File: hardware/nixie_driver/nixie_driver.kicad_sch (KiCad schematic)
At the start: 46 parts, among them J2 Conn_02x05_Odd_Even, U8 CD40109B, U9 TubeClock_HV5622

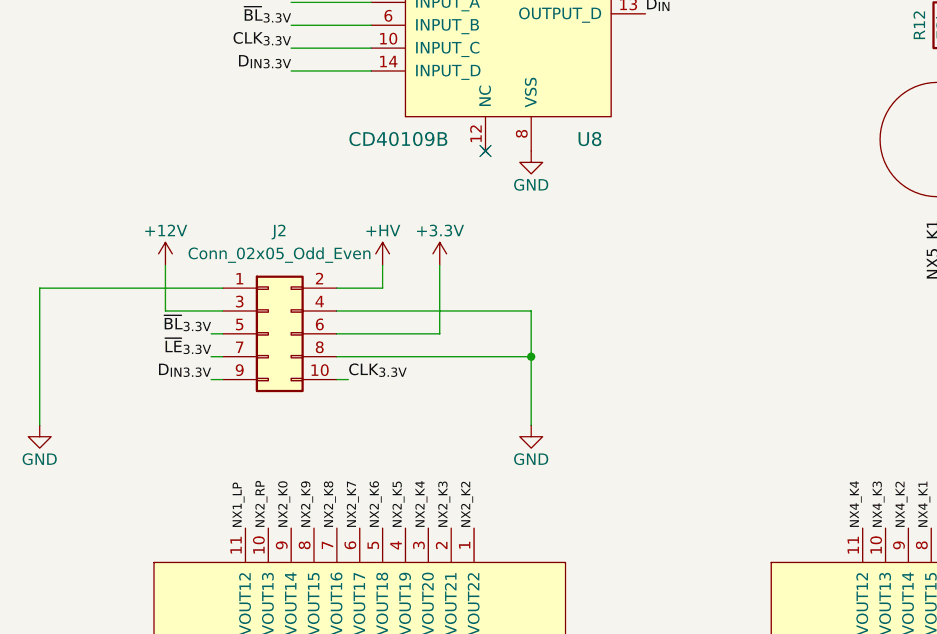
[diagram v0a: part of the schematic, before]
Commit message: Changed connectors to driver board, fixed oscillator connections
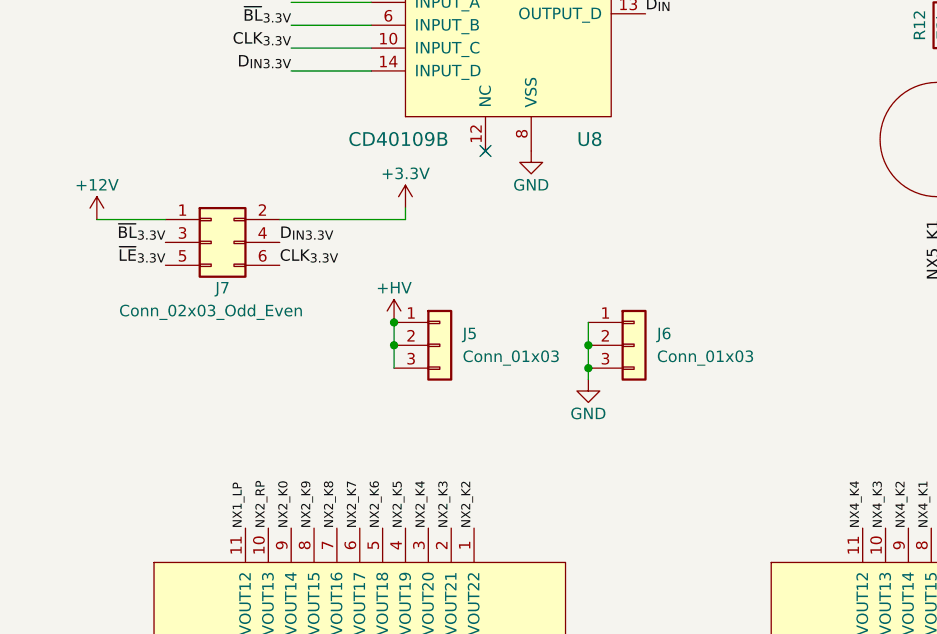
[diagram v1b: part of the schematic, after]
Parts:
- removed J2: Conn_02x05_Odd_Even, Connector_PinHeader_2.54mm:PinHeader_2x05_P2.54mm_Vertical, symbol Connector_Generic:Conn_02x05_Odd_Even
- added J5, J6: Conn_01x03, Connector_PinHeader_2.54mm:PinHeader_1x03_P2.54mm_Vertical, symbol Connector_Generic:Conn_01x03
- added J7: Conn_02x03_Odd_Even, Connector_PinHeader_2.54mm:PinHeader_2x03_P2.54mm_Vertical, symbol Connector_Generic:Conn_02x03_Odd_Even
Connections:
- net +12V: now also J7.1 (Pin_1)
- net +3V3: now also J7.2 (Pin_2)
- net +HV: now also J5.1 (Pin_1), J5.2 (Pin_2), J5.3 (Pin_3)
- net CLK_{3.3V}: now also J7.6 (Pin_6)
- net D_{IN}_{3.3V}: now also J7.4 (Pin_4)
- net GND: now also J6.1 (Pin_1), J6.2 (Pin_2), J6.3 (Pin_3)
- net ~{BL}_{3.3V}: now also J7.3 (Pin_3)
- net ~{LE}_{3.3V}: now also J7.5 (Pin_5)

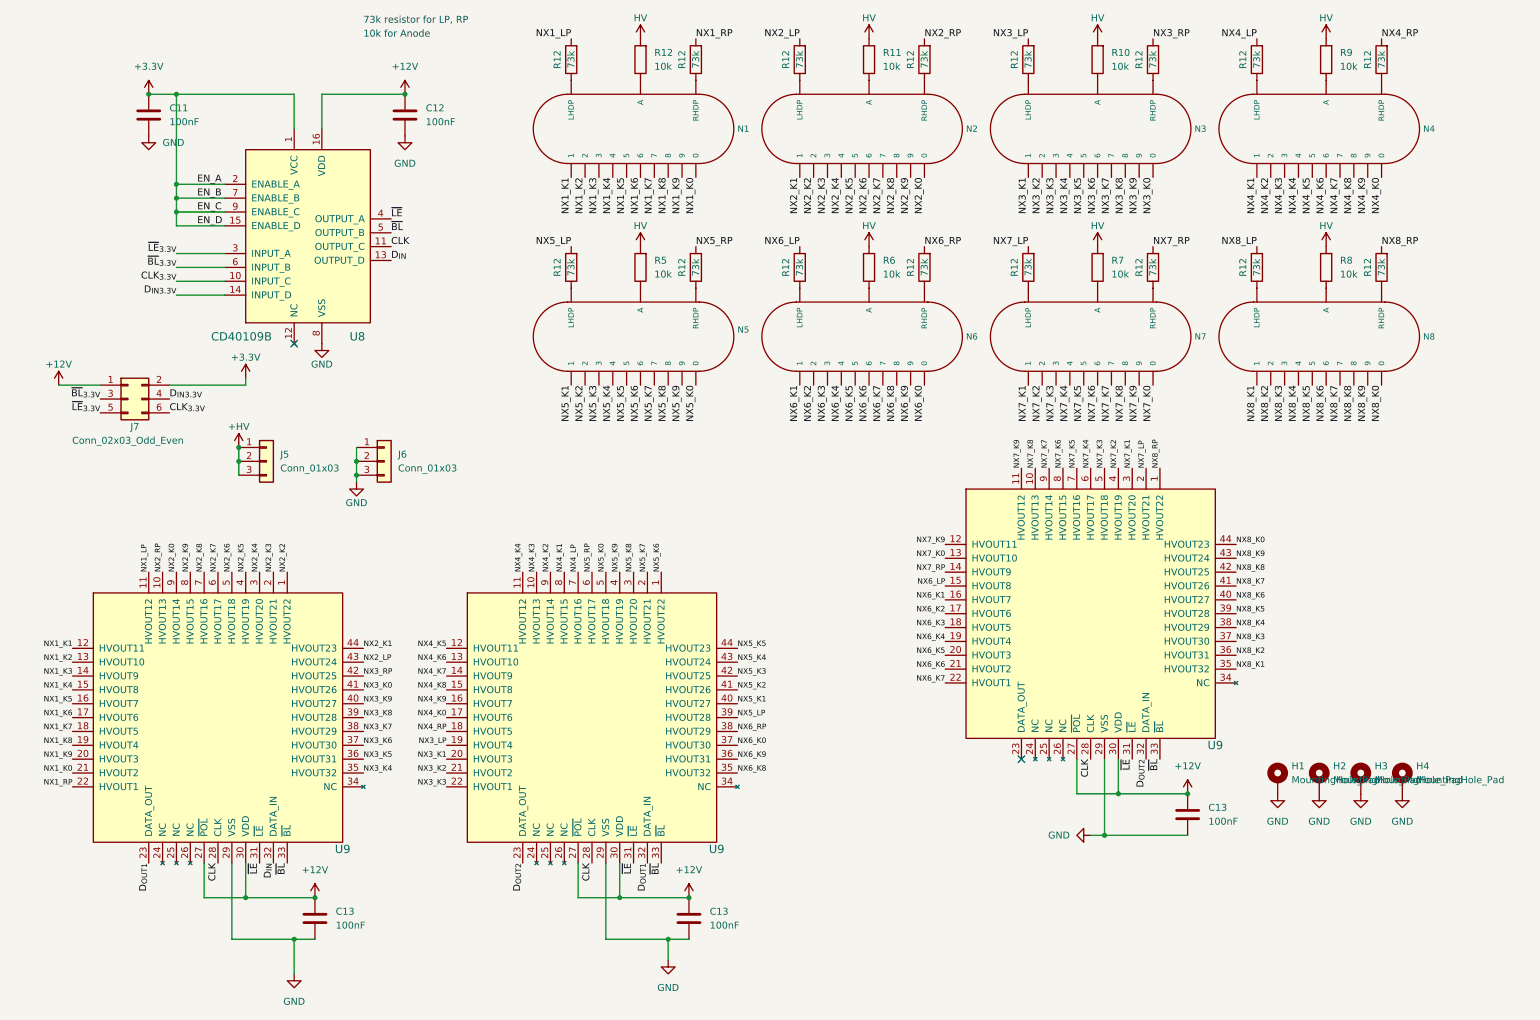
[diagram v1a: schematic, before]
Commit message: Inital PCB placement
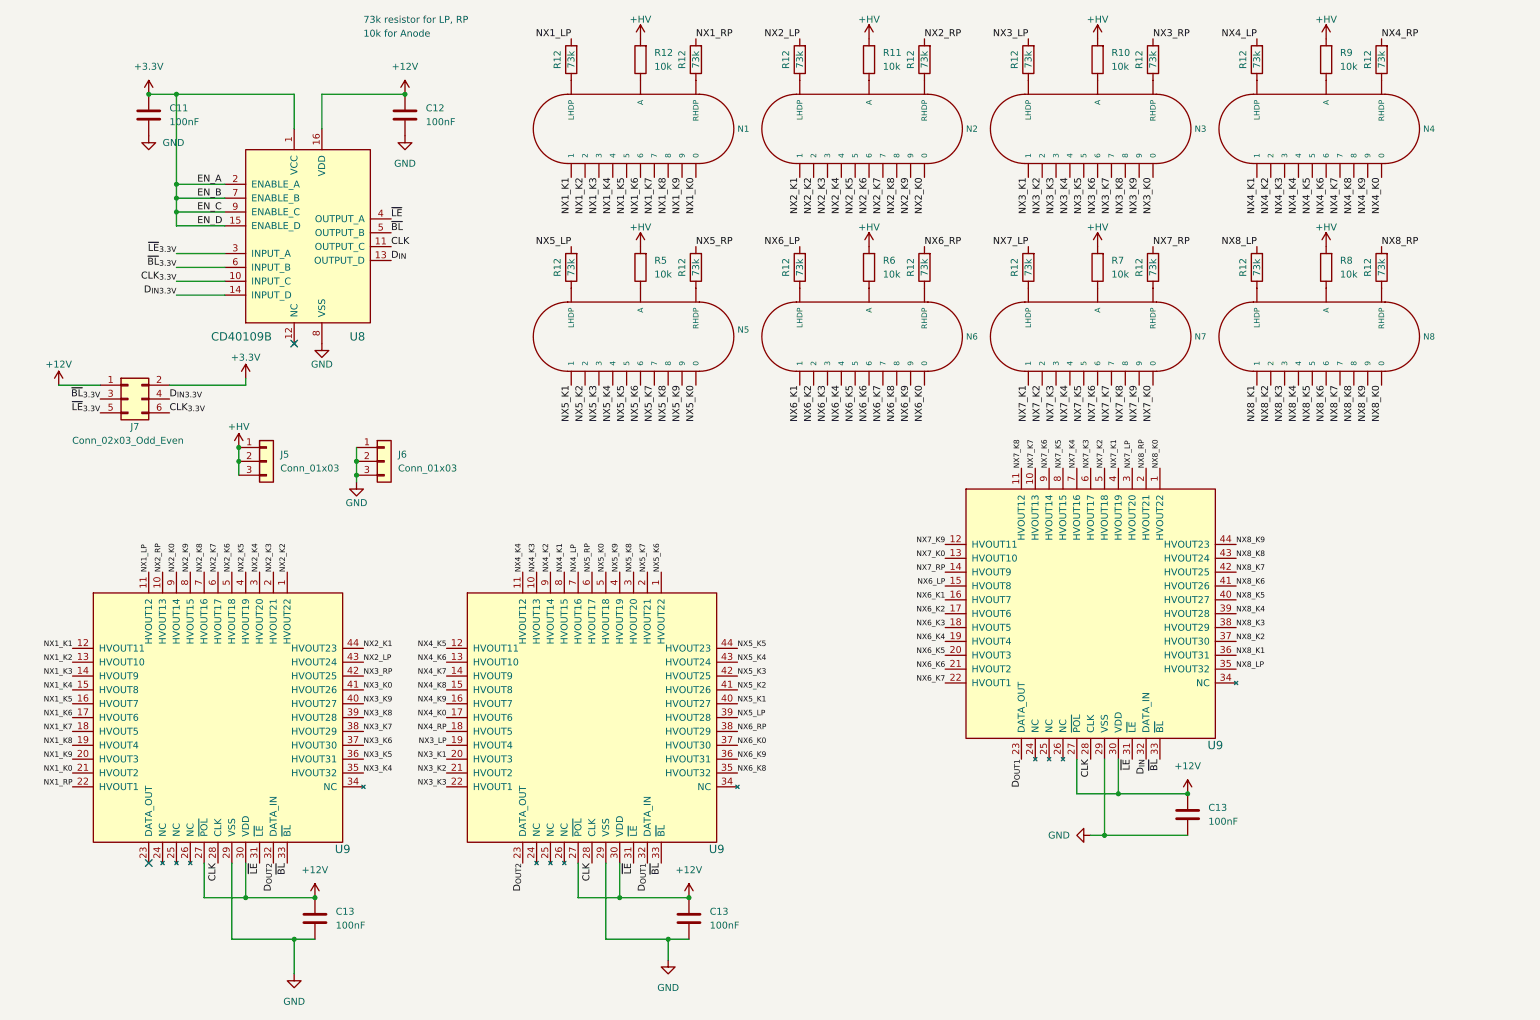
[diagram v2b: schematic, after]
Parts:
- removed H1, H2, H3, H4: MountingHole_Pad, MountingHole:MountingHole_3.2mm_M3_Pad_Via, symbol Mechanical:MountingHole_Pad
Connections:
- net VDD is gone; now on net +HV: R10.2, R11.2, R12.2, R5.2, R6.2, R7.2, R8.2, R9.2
- net D_{IN}: now also U9.32 (DATA_IN); no longer U9.32 (DATA_IN)
- net D_{OUT1}: now also U9.23 (DATA_OUT); no longer U9.23 (DATA_OUT)
- net D_{OUT2}: now also U9.32 (DATA_IN); no longer U9.32 (DATA_IN)
- net NX7_K1: now also U9.4 (HVOUT19); no longer U9.3 (HVOUT20)
- net NX7_K2: now also U9.5 (HVOUT18); no longer U9.4 (HVOUT19)
- net NX7_K3: now also U9.6 (HVOUT17); no longer U9.5 (HVOUT18)
- net NX7_K4: now also U9.7 (HVOUT16); no longer U9.6 (HVOUT17)
- net NX7_K5: now also U9.8 (HVOUT15); no longer U9.7 (HVOUT16)
- net NX7_K6: now also U9.9 (HVOUT14); no longer U9.8 (HVOUT15)
- net NX7_K7: now also U9.10 (HVOUT13); no longer U9.9 (HVOUT14)
- net NX7_K8: now also U9.11 (HVOUT12); no longer U9.10 (HVOUT13)
- net NX7_K9: no longer U9.11 (HVOUT12)
- net NX7_LP: now also U9.3 (HVOUT20); no longer U9.2 (HVOUT21)
- net NX8_K0: now also U9.1 (HVOUT22); no longer U9.44 (HVOUT23)
- net NX8_K1: now also U9.36 (HVOUT31); no longer U9.35 (HVOUT32)
- net NX8_K2: now also U9.37 (HVOUT30); no longer U9.36 (HVOUT31)
- net NX8_K3: now also U9.38 (HVOUT29); no longer U9.37 (HVOUT30)
- net NX8_K4: now also U9.39 (HVOUT28); no longer U9.38 (HVOUT29)
- net NX8_K5: now also U9.40 (HVOUT27); no longer U9.39 (HVOUT28)
- net NX8_K6: now also U9.41 (HVOUT26); no longer U9.40 (HVOUT27)
- net NX8_K7: now also U9.42 (HVOUT25); no longer U9.41 (HVOUT26)
- net NX8_K8: now also U9.43 (HVOUT24); no longer U9.42 (HVOUT25)
- net NX8_K9: now also U9.44 (HVOUT23); no longer U9.43 (HVOUT24)
- net NX8_LP: now also U9.35 (HVOUT32)
- net NX8_RP: now also U9.2 (HVOUT21); no longer U9.1 (HVOUT22)

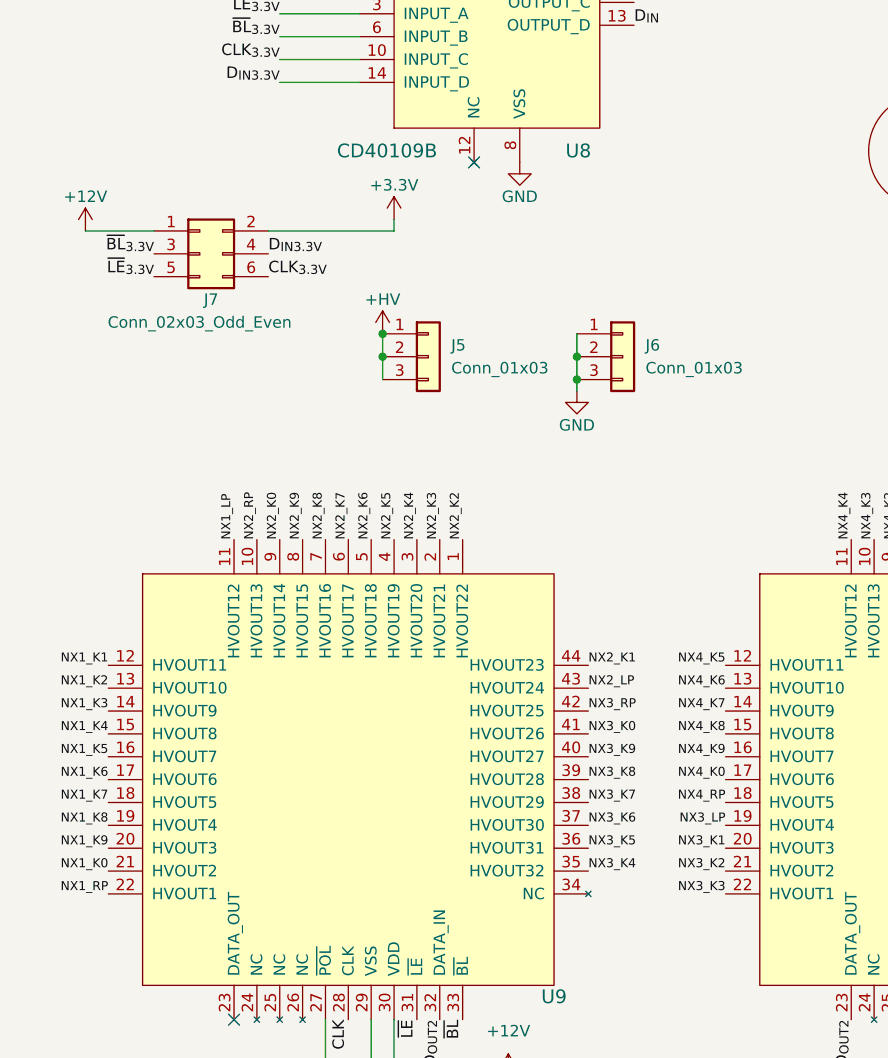
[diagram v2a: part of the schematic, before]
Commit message: PCB layout, traces for nixie_driver, 3 Nixies + logic
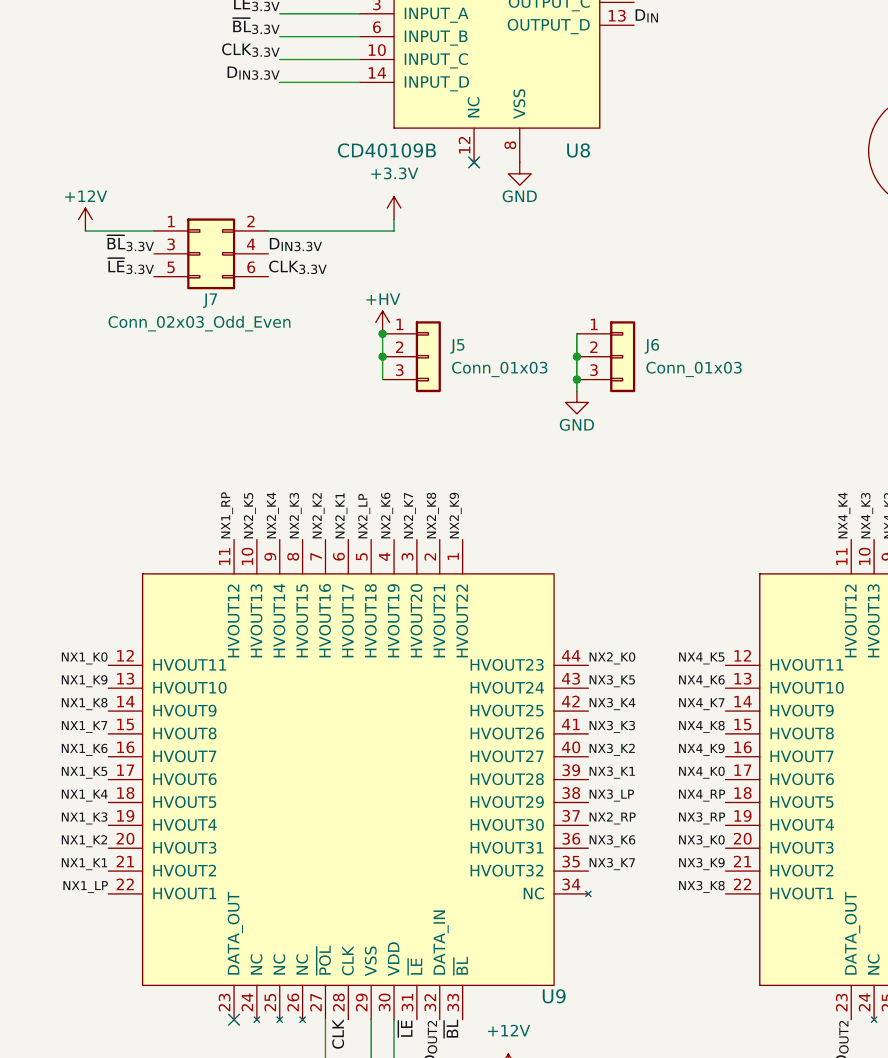
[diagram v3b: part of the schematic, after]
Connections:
- net +3V3 is gone; now on net +3.3V: J7.2 (Pin_2)
- net NX1_K0: now also U9.12 (HVOUT11); no longer U9.21 (HVOUT2)
- net NX1_K1: now also U9.21 (HVOUT2); no longer U9.12 (HVOUT11)
- net NX1_K2: now also U9.20 (HVOUT3); no longer U9.13 (HVOUT10)
- net NX1_K3: now also U9.19 (HVOUT4); no longer U9.14 (HVOUT9)
- net NX1_K4: now also U9.18 (HVOUT5); no longer U9.15 (HVOUT8)
- net NX1_K5: now also U9.17 (HVOUT6); no longer U9.16 (HVOUT7)
- net NX1_K6: now also U9.16 (HVOUT7); no longer U9.17 (HVOUT6)
- net NX1_K7: now also U9.15 (HVOUT8); no longer U9.18 (HVOUT5)
- net NX1_K8: now also U9.14 (HVOUT9); no longer U9.19 (HVOUT4)
- net NX1_K9: now also U9.13 (HVOUT10); no longer U9.20 (HVOUT3)
- net NX1_LP: now also U9.22 (HVOUT1); no longer U9.11 (HVOUT12)
- net NX1_RP: now also U9.11 (HVOUT12); no longer U9.22 (HVOUT1)
- net NX2_K0: now also U9.44 (HVOUT23); no longer U9.9 (HVOUT14)
- net NX2_K1: now also U9.6 (HVOUT17); no longer U9.44 (HVOUT23)
- net NX2_K2: now also U9.7 (HVOUT16); no longer U9.1 (HVOUT22)
- net NX2_K3: now also U9.8 (HVOUT15); no longer U9.2 (HVOUT21)
- net NX2_K4: now also U9.9 (HVOUT14); no longer U9.3 (HVOUT20)
- net NX2_K5: now also U9.10 (HVOUT13); no longer U9.4 (HVOUT19)
- net NX2_K6: now also U9.4 (HVOUT19); no longer U9.5 (HVOUT18)
- net NX2_K7: now also U9.3 (HVOUT20); no longer U9.6 (HVOUT17)
- net NX2_K8: now also U9.2 (HVOUT21); no longer U9.7 (HVOUT16)
- net NX2_K9: now also U9.1 (HVOUT22); no longer U9.8 (HVOUT15)
- net NX2_LP: now also U9.5 (HVOUT18); no longer U9.43 (HVOUT24)
- net NX2_RP: now also U9.37 (HVOUT30); no longer U9.10 (HVOUT13)
- net NX3_K0: now also U9.20 (HVOUT3); no longer U9.41 (HVOUT26)
- net NX3_K1: now also U9.39 (HVOUT28); no longer U9.20 (HVOUT3)
- net NX3_K2: now also U9.40 (HVOUT27); no longer U9.21 (HVOUT2)
- net NX3_K3: now also U9.41 (HVOUT26); no longer U9.22 (HVOUT1)
- net NX3_K4: now also U9.42 (HVOUT25); no longer U9.35 (HVOUT32)
- net NX3_K5: now also U9.43 (HVOUT24); no longer U9.36 (HVOUT31)
- net NX3_K6: now also U9.36 (HVOUT31); no longer U9.37 (HVOUT30)
- net NX3_K7: now also U9.35 (HVOUT32); no longer U9.38 (HVOUT29)
- net NX3_K8: now also U9.22 (HVOUT1); no longer U9.39 (HVOUT28)
- net NX3_K9: now also U9.21 (HVOUT2); no longer U9.40 (HVOUT27)
- net NX3_LP: now also U9.38 (HVOUT29); no longer U9.19 (HVOUT4)
- net NX3_RP: now also U9.19 (HVOUT4); no longer U9.42 (HVOUT25)
